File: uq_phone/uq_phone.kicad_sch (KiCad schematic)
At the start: 0 parts

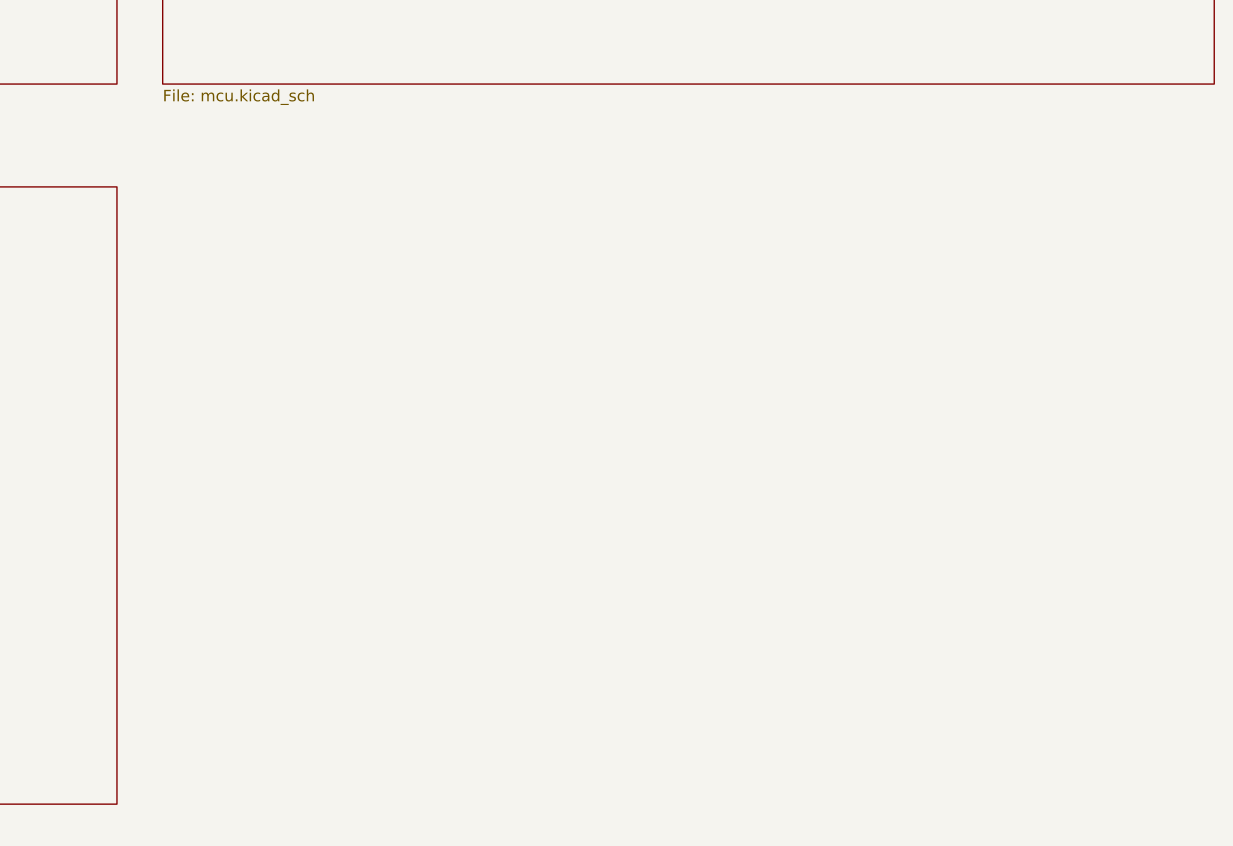
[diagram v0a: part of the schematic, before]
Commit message: Add LEDs, Inital Buttons
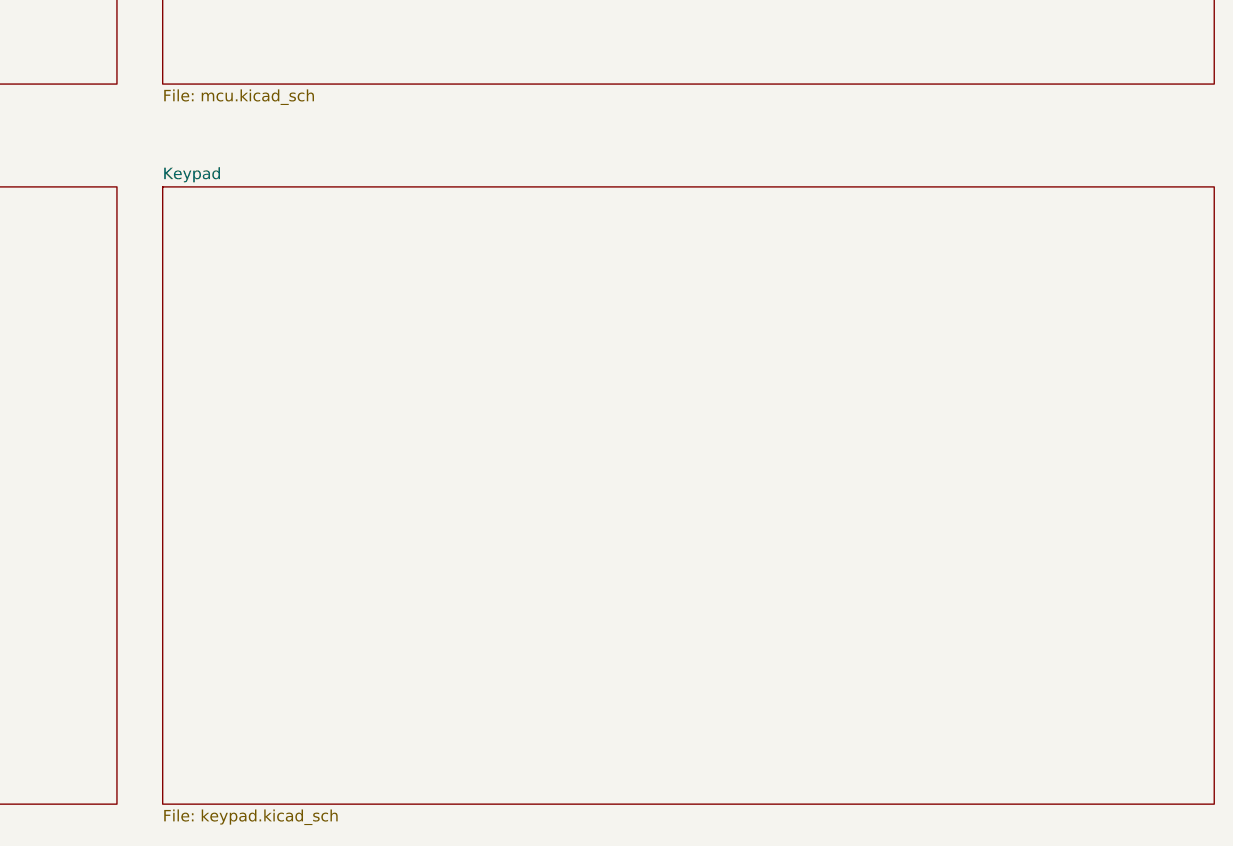
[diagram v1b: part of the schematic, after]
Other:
- added sheet Keypad (keypad.kicad_sch)
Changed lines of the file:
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@@
+		)
+	)
+	(sheet
+		(at 261.62 96.52)
+		(size 116.84 68.58)
+		(fields_autoplaced yes)
+		(stroke
+			(width 0.1524)
+			(type solid)
+		)
+		(fill
+			(color 0 0 0 0.0000)
+		)
+		(property "Sheetname" "Keypad"
+			(at 261.62 95.8084 0)
+			(effects
+				(font
+					(size 1.27 1.27)
+				)
+				(justify left bottom)
+			)
+		)
+		(property "Sheetfile" "keypad.kicad_sch"
+			(at 261.62 165.6846 0)
+			(effects
+				(font
+					(size 1.27 1.27)
+				)
+				(justify left top)
+			)
+		)
+		(instances
+			(project "uq_phone"
+				(path "/14f57415-6807-40a5-bb38-3cb818a2cdae"
+					(page "7")
+				)
+			)
 		)
 	)
